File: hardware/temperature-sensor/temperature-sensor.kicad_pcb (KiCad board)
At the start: 4 copper layers, 56 x 56 mm, 126 parts, among them IC1 SHT40-CD1B-R3, IC2 MAX5969BETB+T, IC3 LV2862XLVDDCR, IC4 LV2862XLVDDCR, J1 1149611, J2 219320-0001, J3 1990012, J4 ARM-JTAG-SWD, Q1 DMN3404L, Q2 DMN3404L, Q3 DMN3404L, Q4 DMN3404L, T1 SM13126PEL, U1 STM32F407V_E-G_Tx, U2 LAN8720A, U3 FT230XS, U4 AT24C512C, Y1 CX2016FB25000C0FZZH1

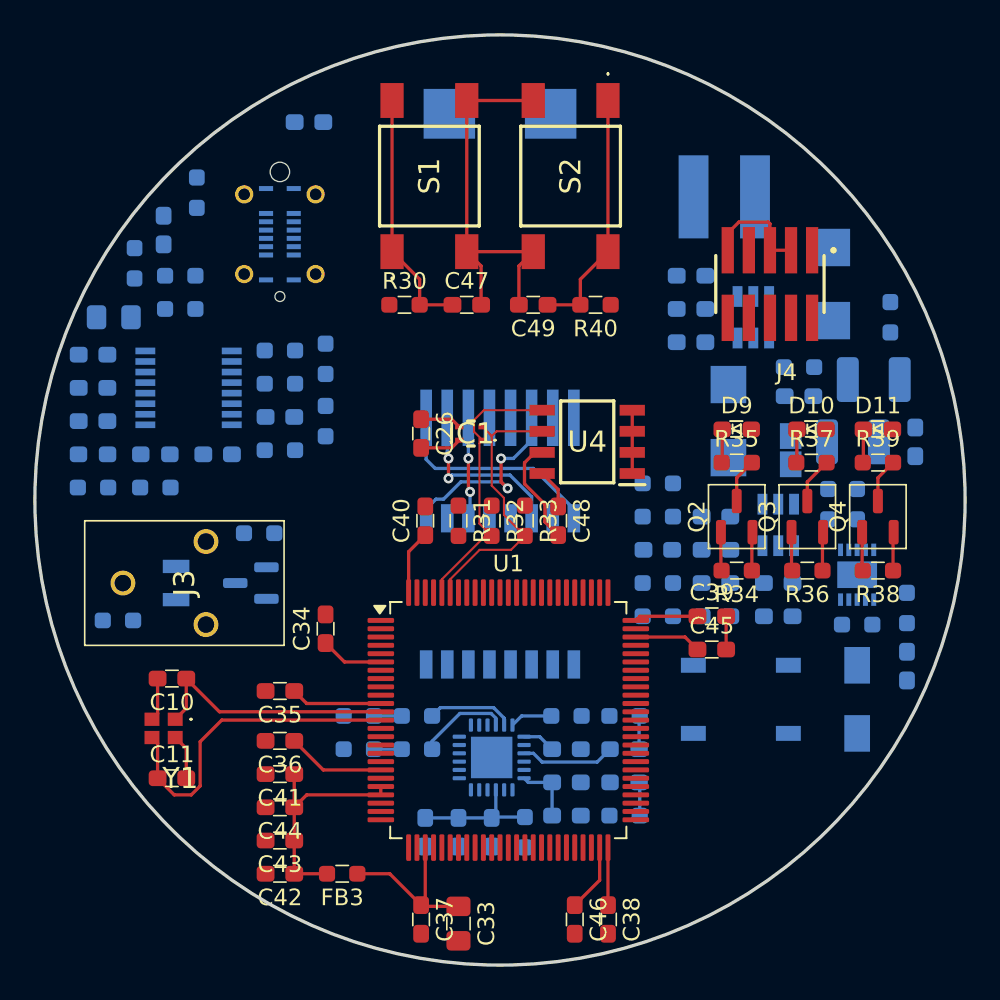
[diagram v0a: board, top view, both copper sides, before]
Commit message: route temperature sensor
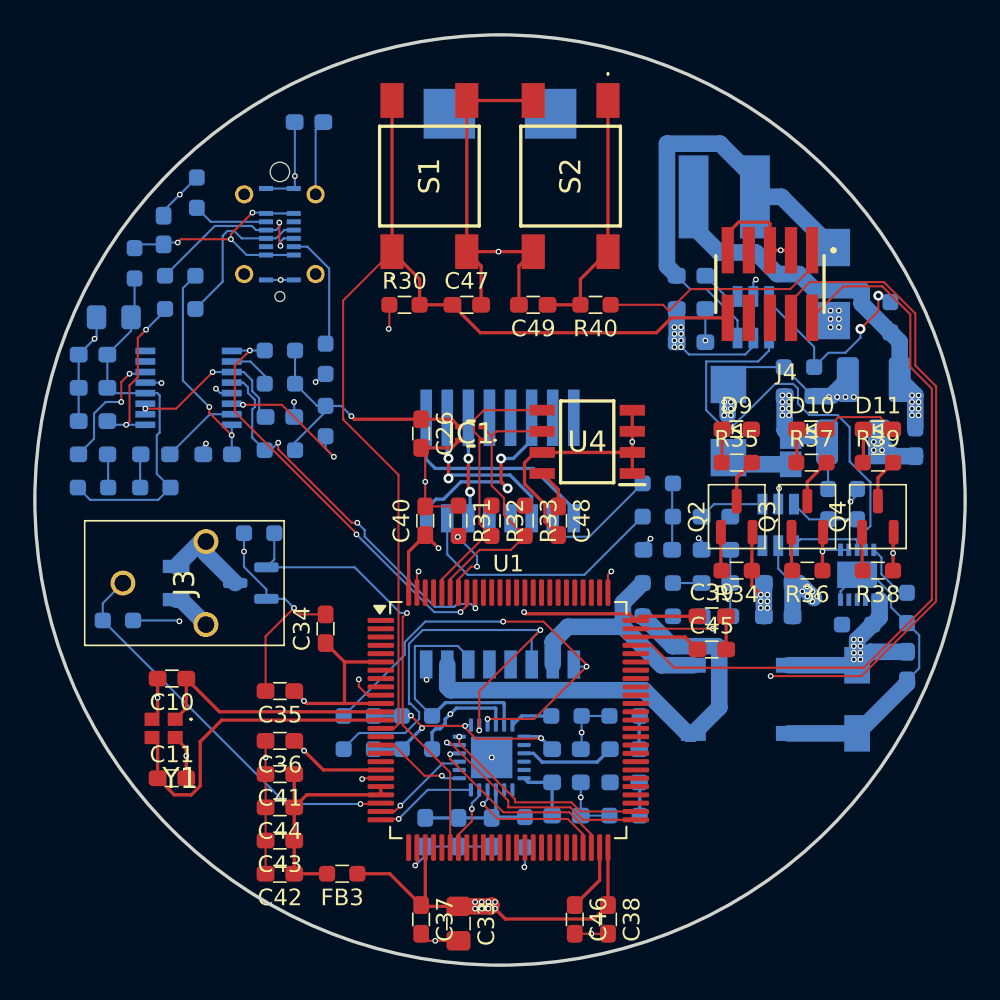
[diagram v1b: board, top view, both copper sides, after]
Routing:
- net /3V3: track 41.8 -> 218.9 mm, vias 0 -> 24
- net GND: track 58.1 -> 166.6 mm, vias 0 -> 62
- net /12V: track 0.00 -> 82.4 mm, vias 0 -> 8
- net /MCU/SWCLK: track 0.00 -> 53.0 mm, vias 0 -> 2
- net /Power over Ethernet/54V: track 0.00 -> 52.2 mm, vias 0 -> 22
- net /MCU/NRST: track 15.0 -> 64.8 mm
- net /MCU/SWDIO: track 0.00 -> 45.2 mm
- net /Power over Ethernet/PG: track 0.00 -> 31.7 mm
- net /Ethernet/TX_N: track 0.00 -> 28.6 mm, vias 0 -> 2
- net /Ethernet/CT2: track 0.00 -> 28.5 mm
- net /Fan/PWM: track 0.00 -> 27.3 mm, vias 0 -> 1
- net Net-(D4-K): track 0.00 -> 27.2 mm
- net /Ethernet/TX_P: track 0.00 -> 26.7 mm, vias 0 -> 3
- net /MCU/UART_RX: track 0.00 -> 25.8 mm, vias 0 -> 3
- net /Fan/TACH: track 0.00 -> 24.1 mm, vias 0 -> 1
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
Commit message: add missing routes
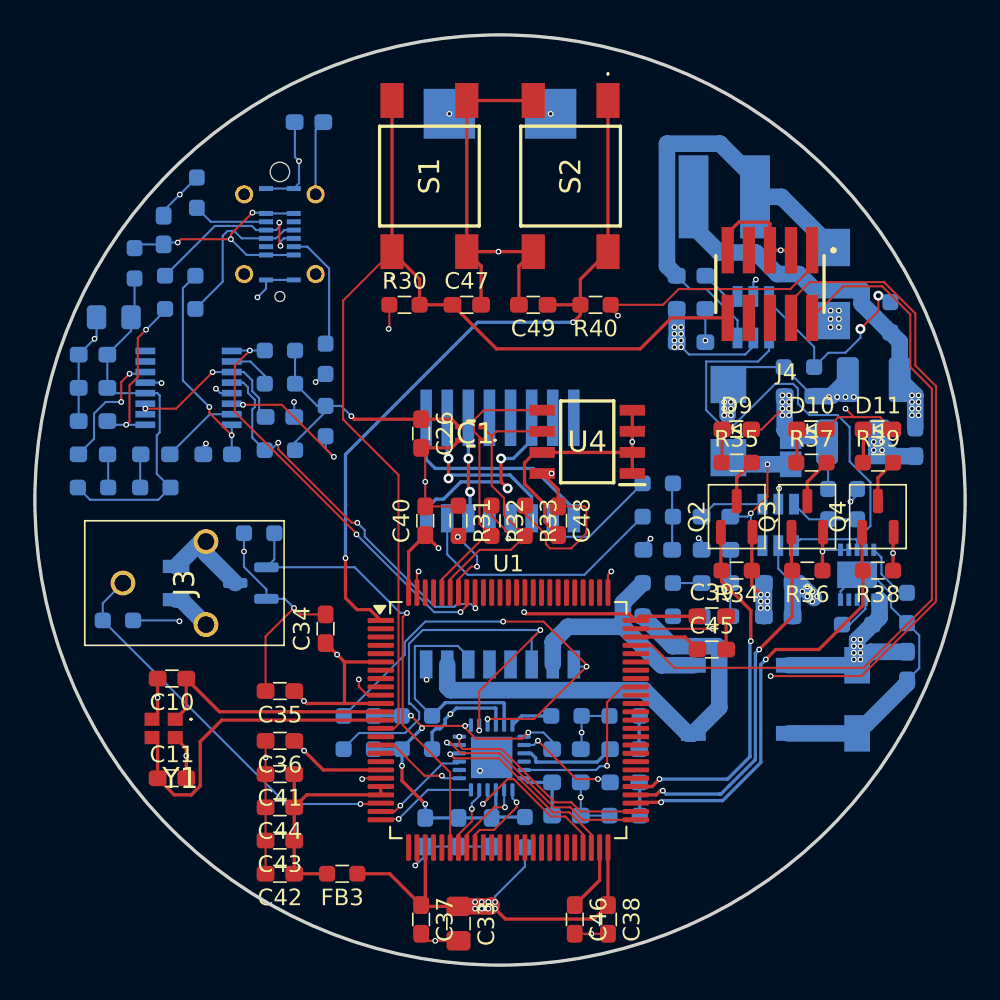
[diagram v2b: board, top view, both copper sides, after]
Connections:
- U1 pad 1: unconnected-(U1-PE2-Pad1) -> /MCU/CONNECT
- U1 pad 26: /MCU/LED1 -> unconnected-(U1-PA3-Pad26)
- U1 pad 29: /MCU/LED2 -> unconnected-(U1-PA4-Pad29)
- U1 pad 30: /MCU/LED3 -> unconnected-(U1-PA5-Pad30)
- U1 pad 53: unconnected-(U1-PB14-Pad53) -> /MCU/LED3
- U1 pad 54: unconnected-(U1-PB15-Pad54) -> /MCU/LED2
- U1 pad 55: unconnected-(U1-PD8-Pad55) -> /MCU/LED1
- U1 pad 68: /MCU/CONNECT -> unconnected-(U1-PA9-Pad68)
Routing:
- net /3V3: track 218.9 -> 252.1 mm, vias 24 -> 28
- net /MCU/CONNECT: track 15.0 -> 44.5 mm, vias 0 -> 2
- net /MCU/LED3: track 2.33 -> 26.5 mm, vias 0 -> 2
- net /MCU/LED2: track 2.33 -> 22.9 mm, vias 0 -> 2
- net /MCU/LED1: track 2.33 -> 21.9 mm, vias 0 -> 2
- net /Ethernet/25MHz: track 0.00 -> 11.1 mm, vias 0 -> 1
- net Net-(D7-K): track 3.92 -> 10.8 mm, vias 0 -> 2
- net Net-(D2-A): track 0.00 -> 6.32 mm, vias 0 -> 2
- net /Ethernet/RXD1/MODE1: track 0.00 -> 5.11 mm, vias 0 -> 1
- net /Ethernet/RXD0/MODE0: track 0.00 -> 4.83 mm, vias 0 -> 1
- net Net-(U2-VDD1A): track 24.4 -> 28.9 mm, vias 4 -> 6
- net Net-(IC2-DET): track 0.00 -> 2.36 mm
- net Net-(C12-Pad1): track 0.00 -> 1.72 mm
- net GND: track 166.6 -> 168.1 mm, vias 62 -> 64
- net /Ethernet/RXER/PHYAD0: track 8.55 -> 9.79 mm
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
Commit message: fix DRC errors
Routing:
- net GND: track 168.1 -> 170.4 mm, vias 64 -> 63
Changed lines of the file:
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@@
 	)
 	(footprint "benediktibk:INDPM2012X120N"
-		(placed yes)
 		(layer "B.Cu")
 		(at 167.5 96 90)
@@
 		)
 		(pad "1" smd rect
-			(at -0.85 0)
-			(size 1.3 1.55)
+			(at -0.9625 0)
+			(size 1.3 1.325)
 			(layers "B.Cu" "B.Paste" "B.Mask")
 			(net 151 "Net-(D7-K)")
@@
 		)
 		(pad "2" smd rect
-			(at 0.85 0)
-			(size 1.3 1.55)
+			(at 0.9125 0)
+			(size 1.3 1.425)
 			(layers "B.Cu" "B.Paste" "B.Mask")
 			(net 4 "/3V3")
@@
 	)
 	(segment
-		(start 162.8 106.75)
-		(end 162.8625 106.75)
-		(width 0.127)
-		(layer "F.Cu")
-		(net 1)
-	)
-	(segment
 		(start 131.1125 113.9625)
 		(end 130.45 113.3)
@@
 	)
 	(segment
-		(start 162.8625 106.75)
-		(end 163.6125 106)
-		(width 0.127)
-		(layer "F.Cu")
-		(net 1)
-	)
-	(segment
 		(start 146.1 125.5375)
 		(end 145.675 125.5375)
@@
 	)
 	(segment
+		(start 163.6125 106)
+		(end 165.2 106)
+		(width 0.127)
+		(layer "F.Cu")
+		(net 1)
+	)
+	(segment
 		(start 165.1625 104.1625)
 		(end 165.7 104.7)
@@
 	)
 	(segment
+		(start 158.175 106.75)
+		(end 162.8625 106.75)
+		(width 0.127)
+		(layer "F.Cu")
+		(net 1)
+	)
+	(segment
 		(start 173.6625 103.25)
 		(end 173.6625 102.2)
@@
 	)
 	(segment
+		(start 165.2 106)
+		(end 165.7 105.5)
+		(width 0.127)
+		(layer "F.Cu")
+		(net 1)
+	)
+	(segment
 		(start 147.0875 95.8625)
 		(end 147.55 95.4)
@@
 	)
 	(segment
+		(start 162.8625 106.75)
+		(end 163.6125 106)
+		(width 0.127)
+		(layer "F.Cu")
+		(net 1)
+	)
+	(segment
 		(start 163.6125 106)
 		(end 163.6125 108)
@@
 	)
 	(segment
-		(start 158.175 106.75)
-		(end 162.8 106.75)
-		(width 0.127)
-		(layer "F.Cu")
-		(net 1)
-	)
-	(segment
 		(start 167.52 83.965)
 		(end 166.9 83.965)
@@
 	)
 	(via
-		(at 162.8 106.75)
-		(size 0.35)
-		(drill 0.2)
-		(layers "F.Cu" "B.Cu")
-		(net 1)
-	)
-	(via
 		(at 173 95.5)
 		(size 0.35)
@@
 	)
 	(segment
-		(start 149.75 111.55)
-		(end 149.75 112.55)
-		(width 0.2)
-		(layer "B.Cu")
-		(net 86)
-	)
-	(segment
-		(start 147.373 111.527)
-		(end 149.727 111.527)
-		(width 0.2)
+		(start 149.462573 111.527)
+		(end 147.373 111.527)
+		(width 0.127)
 		(layer "B.Cu")
 		(net 86)
@@
 	)
 	(segment
-		(start 149.727 111.527)
-		(end 149.75 111.55)
-		(width 0.2)
-		(layer "B.Cu")
-		(net 86)
-	)
-	(segment
 		(start 145.9125 114)
 		(end 145.9125 112.9875)
@@
 	)
 	(segment
-		(start 147.01 111.89)
-		(end 147.373 111.527)
-		(width 0.2)
+		(start 149.775699 112.524301)
+		(end 149.775699 111.840126)
+		(width 0.127)
+		(layer "B.Cu")
+		(net 86)
+	)
+	(segment
+		(start 149.75 112.55)
+		(end 149.775699 112.524301)
+		(width 0.127)
 		(layer "B.Cu")
 		(net 86)
@@
 	)
 	(segment
+		(start 149.775699 111.840126)
+		(end 149.462573 111.527)
+		(width 0.127)
+		(layer "B.Cu")
+		(net 86)
+	)
+	(segment
+		(start 147.373 111.527)
+		(end 147.01 111.89)
+		(width 0.127)
+		(layer "B.Cu")
+		(net 86)
+	)
+	(segment
 		(start 150.2 111.2)
 		(end 150.25 111.25)
@@
 	)
 	(segment
-		(start 149.25 112.18)
-		(end 152.06 112.18)
+		(start 149.417658 112.18)
+		(end 149.282199 112.044541)
 		(width 0.127)
 		(layer "F.Cu")
@@
 		(net 91)
 	)
+	(segment
+		(start 152.06 112.18)
+		(end 149.417658 112.18)
+		(width 0.127)
+		(layer "F.Cu")
+		(net 91)
+	)
 	(via
 		(at 155.21 109.03)
@@
 	)
 	(via
-		(at 150.19 106.32)
+		(at 149.282199 112.044541)
 		(size 0.35)
 		(drill 0.2)
@@
 	)
 	(via
-		(at 149.25 112.18)
+		(at 150.19 106.32)
 		(size 0.35)
 		(drill 0.2)
@@
 	)
 	(segment
-		(start 132.5 93.4)
-		(end 132.5 93.75)
+		(start 132.25 93.15)
+		(end 132.25 93.5)
 		(width 0.127)
 		(layer "F.Cu")
@@
 	)
 	(segment
-		(start 132.5 93.75)
+		(start 132.25 93.5)
 		(end 133.85 95.1)
 		(width 0.127)
@@
 	)
 	(via
-		(at 132.5 93.4)
+		(at 132.25 93.15)
 		(size 0.35)
 		(drill 0.2)
@@
 	)
 	(segment
-		(start 130.9115 91.8115)
-		(end 132.5 93.4)
+		(start 132.25 93.15)
+		(end 130.9115 91.8115)
 		(width 0.127)
 		(layer "B.Cu")
@@
 	)
 	(segment
-		(start 131.6625 85.5)
-		(end 130.9115 86.251)
+		(start 133.85 94.4725)
+		(end 133.85 95.1)
 		(width 0.127)
 		(layer "B.Cu")
@@
 	)
 	(segment
-		(start 130.9115 86.251)
-		(end 130.9115 91.8115)
+		(start 130.9115 91.8115)
+		(end 130.9115 86.251)
 		(width 0.127)
 		(layer "B.Cu")
@@
 	)
 	(segment
-		(start 133.85 94.4725)
-		(end 133.85 95.1)
+		(start 130.9115 86.251)
+		(end 131.6625 85.5)
 		(width 0.127)
 		(layer "B.Cu")
@@
 	)
 	(segment
-		(start 159.15 116.25)
-		(end 158.175 116.25)
+		(start 164.375233 104.924767)
+		(end 163.3375 103.887034)
 		(width 0.2)
 		(layer "F.Cu")
@@
 	)
 	(segment
-		(start 165.1 105.649534)
-		(end 165.1 107.5)
+		(start 163.3375 103.887034)
+		(end 163.3375 103.25)
+		(width 0.2)
+		(layer "F.Cu")
+		(net 161)
+	)
+	(segment
+		(start 159.15 116.25)
+		(end 158.175 116.25)
 		(width 0.2)
 		(layer "F.Cu")
@@
 		(net 161)
 	)
-	(segment
-		(start 163.3375 103.887034)
-		(end 165.1 105.649534)
-		(width 0.2)
-		(layer "F.Cu")
-		(net 161)
-	)
-	(segment
-		(start 163.3375 103.25)
-		(end 163.3375 103.887034)
-		(width 0.2)
-		(layer "F.Cu")
-		(net 161)
-	)
 	(via
 		(at 159.6 115.8)
@@
 	)
 	(via
-		(at 165.1 107.5)
+		(at 164.375233 104.924767)
 		(size 0.35)
 		(drill 0.2)
@@
 	)
 	(segment
-		(start 163.7 115.8)
-		(end 159.6 115.8)
+		(start 164.375233 104.924767)
+		(end 165.046 105.595534)
 		(width 0.2)
 		(layer "B.Cu")
@@
 	)
 	(segment
-		(start 165.046 107.554)
-		(end 165.046 114.4)
-		(width 0.2)
-		(layer "B.Cu")
-		(net 161)
-	)
-	(segment
-		(start 165.1 107.5)
-		(end 165.046 107.554)
+		(start 163.7 115.8)
+		(end 159.6 115.8)
 		(width 0.2)
 		(layer "B.Cu")
@@
 	)
 	(segment
-		(start 165.046 114.4)
+		(start 165.046 105.595534)
 		(end 165.046 114.454)
 		(width 0.2)

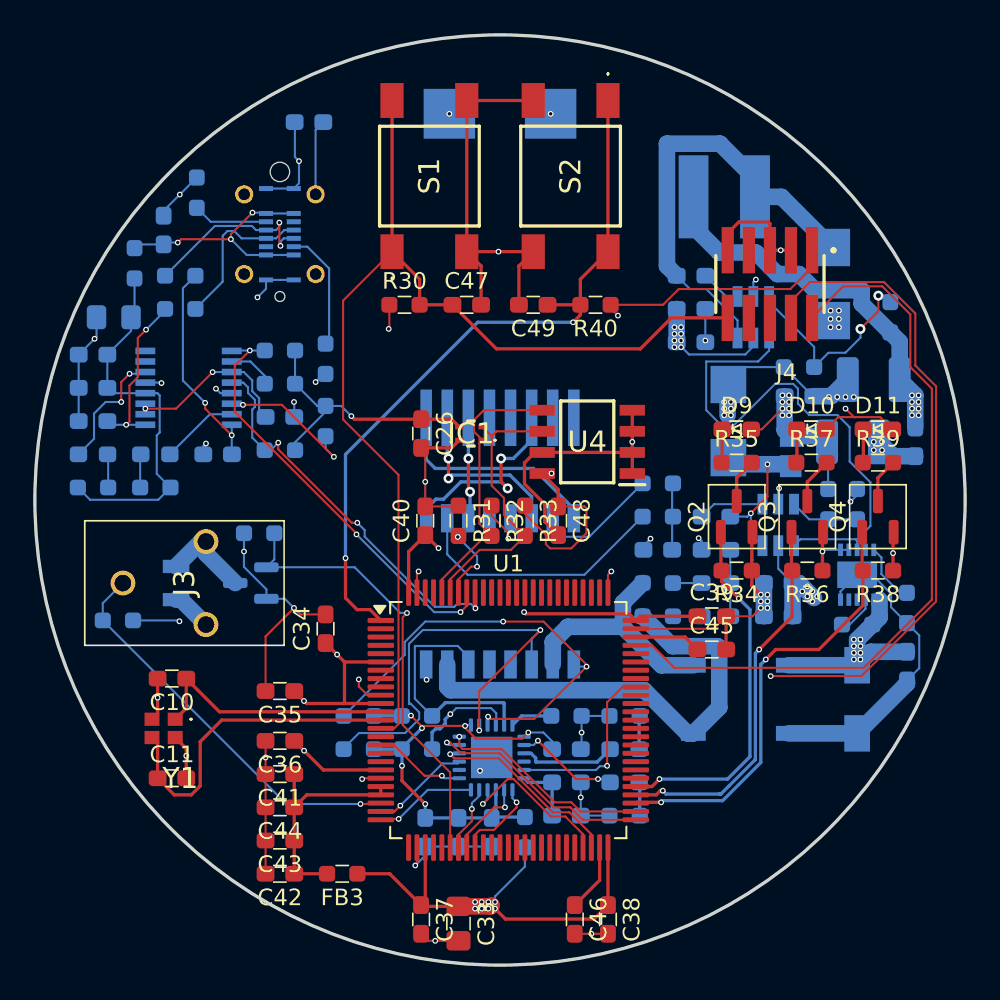
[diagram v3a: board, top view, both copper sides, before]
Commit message: fix silkscreen
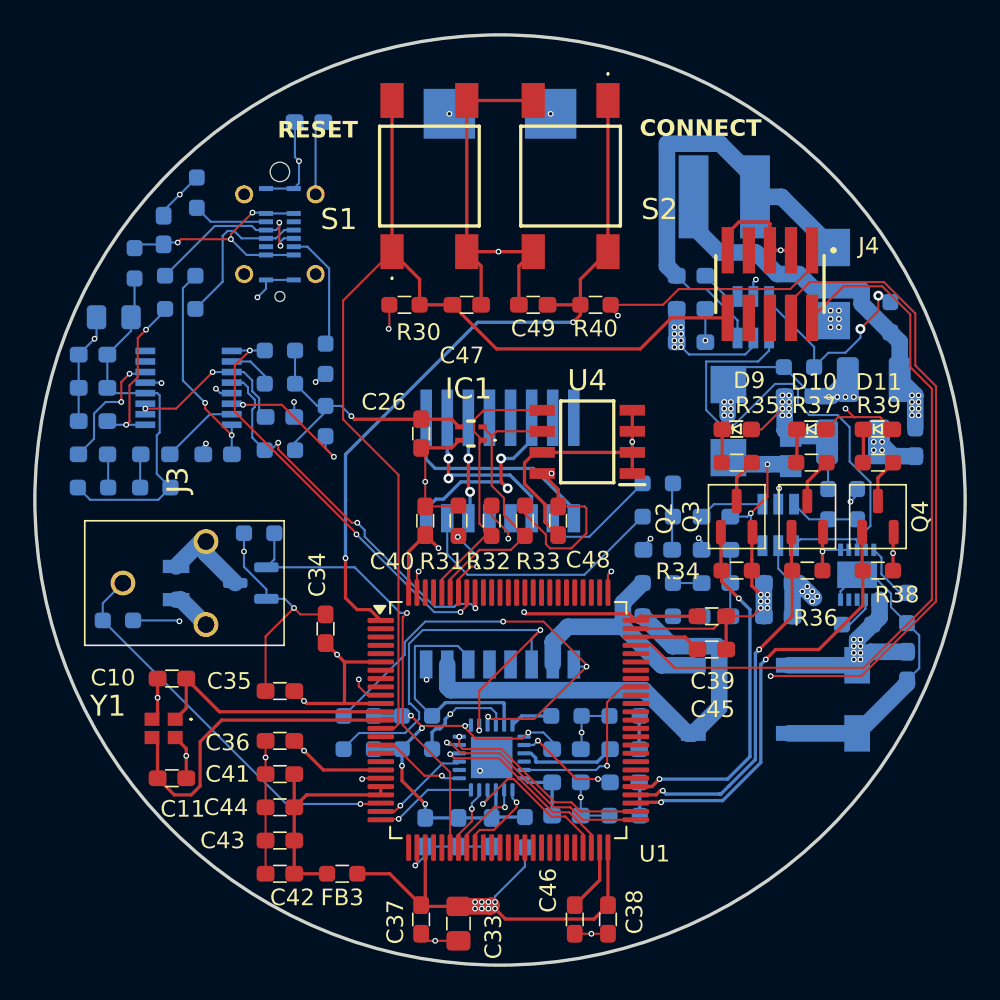
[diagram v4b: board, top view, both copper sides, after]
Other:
- board text added: "CONNECT"
- board text added: "RESET"

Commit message: update PCB from schematic
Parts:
- S2: value RESET -> CONNECT
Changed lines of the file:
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@@
 			)
 		)
-		(property "Value" "RESET"
+		(property "Value" "CONNECT"
 			(at 0 0 90)
 			(layer "F.SilkS")

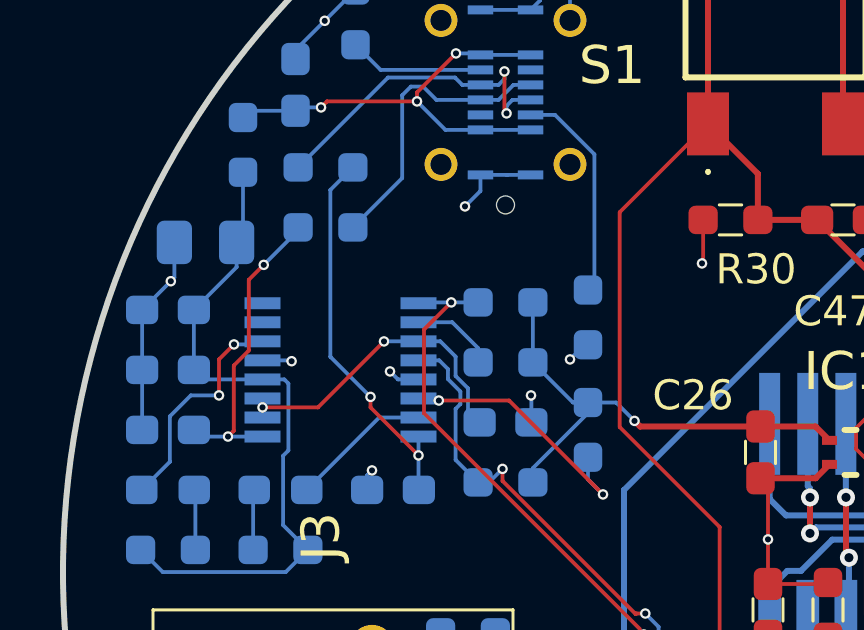
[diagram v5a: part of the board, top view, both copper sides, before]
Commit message: fix silkscreen
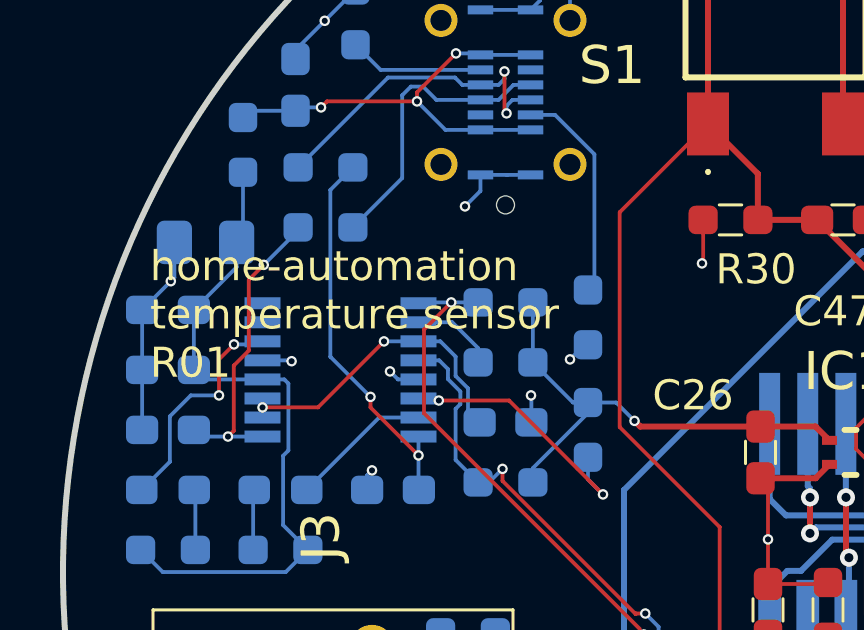
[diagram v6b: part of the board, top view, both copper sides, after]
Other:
- board text added: "home-automation temperature sensor R01"
- board text removed: "TEMP-SENSOR R01"
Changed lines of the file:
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@@
 		)
 	)
-	(gr_text "TEMP-SENSOR R01"
-		(at 160.5 88.75 90)
-		(layer "User.9")
+	(gr_text "home-automation\ntemperature sensor\nR01"
+		(at 124.9 92.6 0)
+		(layer "F.SilkS")
 		(effects
 			(font
